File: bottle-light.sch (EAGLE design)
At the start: 55 parts, among them IC1 STM32F334K8T, IC2 LF33, X1 MINI-USB-SHIELD-UX60A-MB-5ST

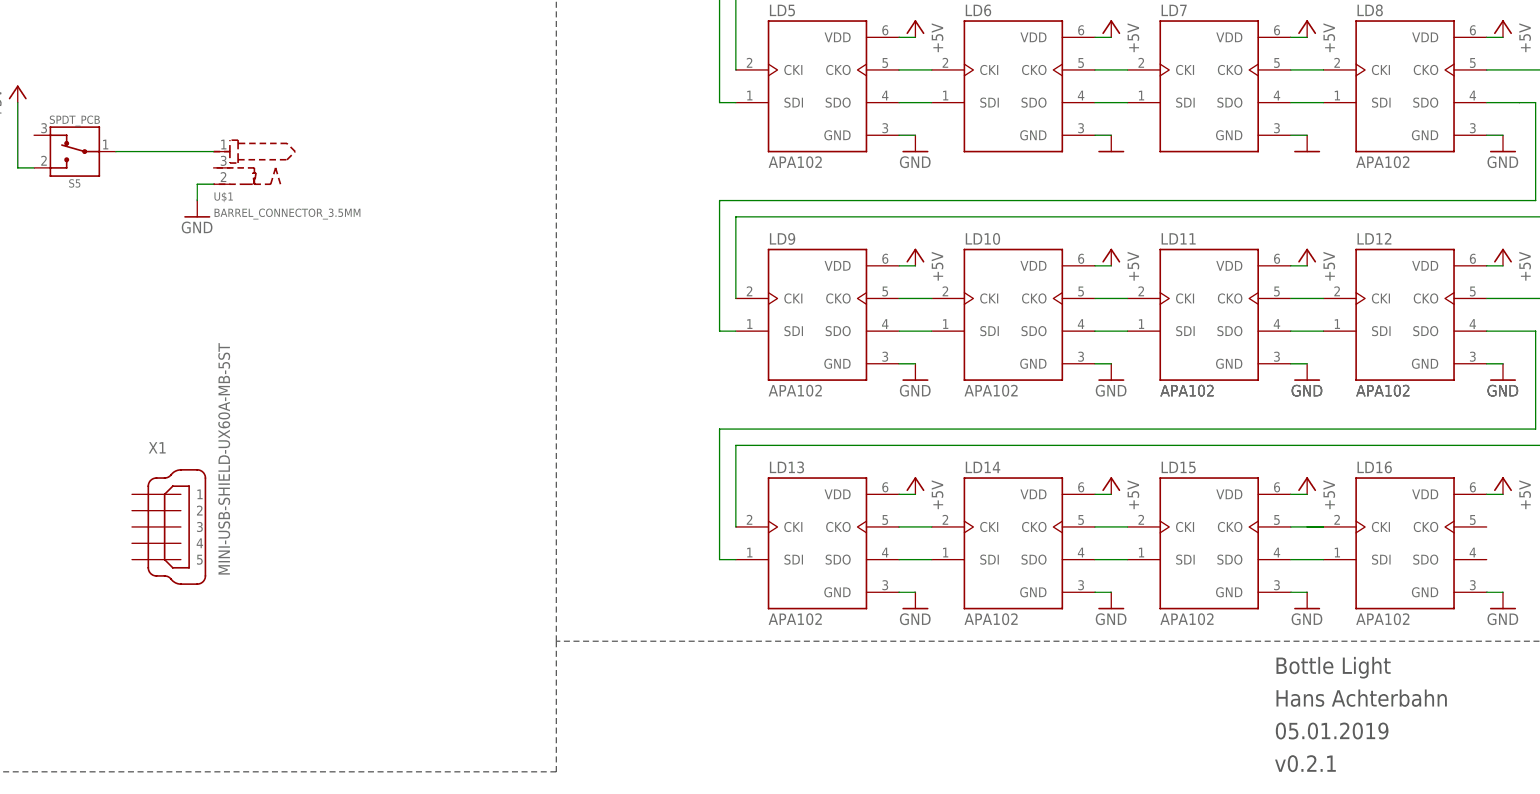
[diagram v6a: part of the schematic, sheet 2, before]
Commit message: v0.2.2 LEDs connected and port for touch pad added
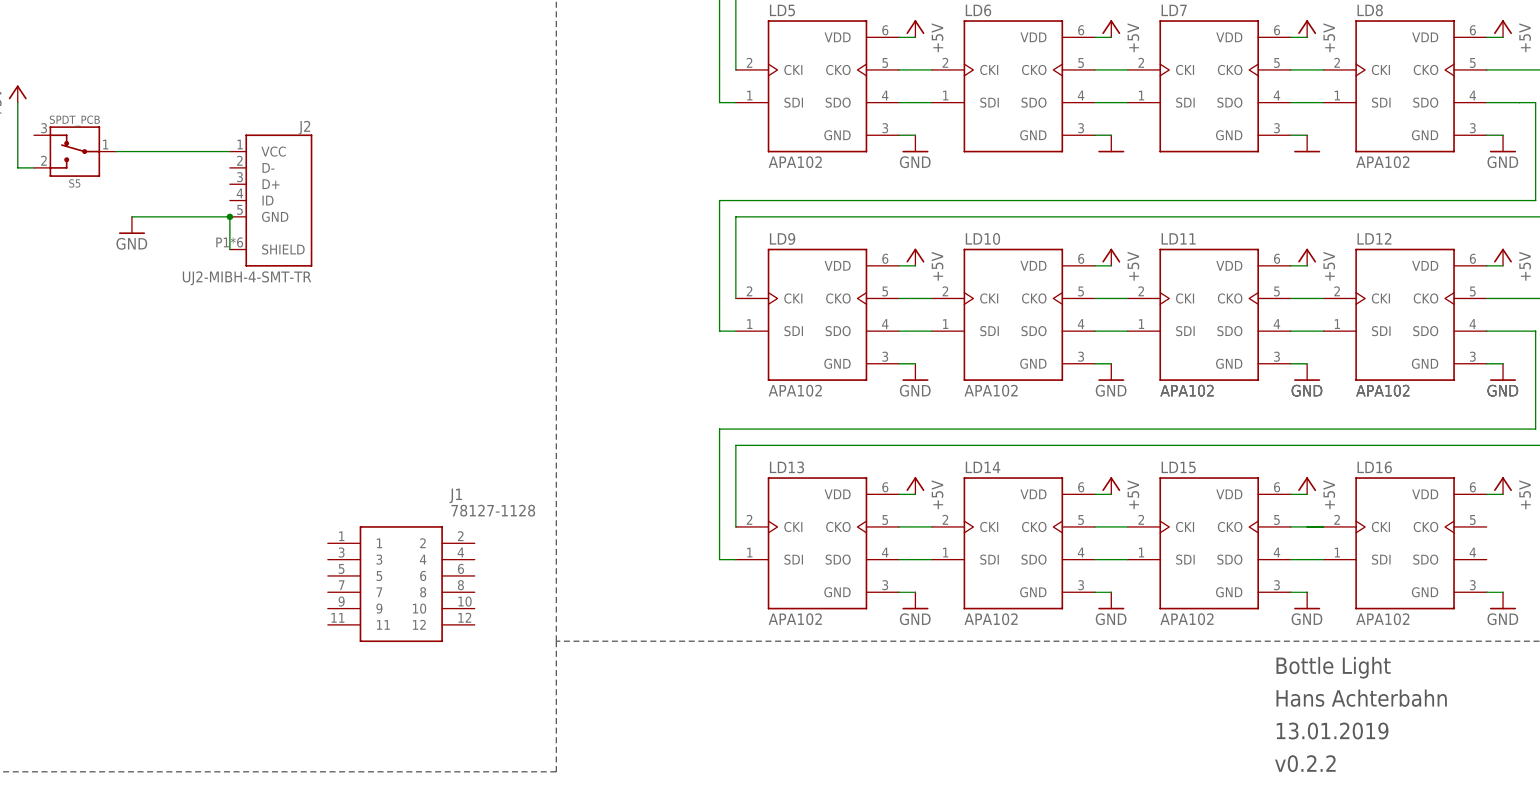
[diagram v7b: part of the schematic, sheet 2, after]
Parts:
- removed U$1: BARREL_CONNECTOR_3.5MM, h8-conector:BARREL_CONNECTOR_3.5MM
- removed X1: MINI-USB-SHIELD-UX60A-MB-5ST, con-hirose:MINI-USB-SHIELD-UX60A-MB-5ST
- added J1: 78127-1128, SamaSys:78127-1128
- added J2: UJ2-MIBH-4-SMT-TR, UJ2-MIBH-4-SMT-TR:UJ2-MIBH-4-SMT-TR
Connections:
- removed net N$76: S5.1, U$1.1
- new net 5V-IN: J2.VCC, S5.1
- net GND: now also J2.GND, J2.SHIELD; no longer U$1.2
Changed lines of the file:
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@@
 <schematic xreflabel="%F%N/%S.%C%R" xrefpart="/%S.%C%R">
 <attributes>
-<attribute name="DATE" value="05.01.2019"/>
+<attribute name="DATE" value="13.01.2019"/>
 <attribute name="EDITOR" value="Hans Achterbahn"/>
 <attribute name="PROJECT" value="Bottle Light"/>
-<attribute name="VERSION" value="v0.2.1"/>
+<attribute name="VERSION" value="v0.2.2"/>
 </attributes>
 <variantdefs>
@@
 <part name="S3" library="h8-switch" deviceset="ALPS-SKHH" device=""/>
 <part name="S4" library="h8-switch" deviceset="ALPS-SKHH" device=""/>
-<part name="U$1" library="h8-conector" deviceset="BARREL_CONNECTOR_3.5MM" device=""/>
 <part name="GND22" library="supply1" library_urn="urn:adsk.eagle:library:371" deviceset="GND" device=""/>
 <part name="JP1" library="h8-pinhead" deviceset="PINHD-2X3" device="_2.54-SMD" value="SWD">
@@
 <part name="P+18" library="supply1" library_urn="urn:adsk.eagle:library:371" deviceset="+5V" device=""/>
 <part name="P+19" library="supply1" library_urn="urn:adsk.eagle:library:371" deviceset="+5V" device=""/>
-<part name="X1" library="con-hirose" library_urn="urn:adsk.eagle:library:152" deviceset="MINI-USB-SHIELD-" device="UX60A-MB-5ST" package3d_urn="urn:adsk.eagle:package:7263/1"/>
 <part name="R1" library="resistor" deviceset="R-EU_" device="R0603" value="8.2">
 <attribute name="RS-ONLINE" value="904-5027"/>
@@
 <attribute name="RS-ONLINE" value="904-5027"/>
 </part>
+<part name="J1" library="SamaSys" deviceset="78127-1128" device=""/>
+<part name="J2" library="UJ2-MIBH-4-SMT-TR" deviceset="UJ2-MIBH-4-SMT-TR" device=""/>
 </parts>
 <sheets>
@@
 <attribute name="VALUE" x="10.16" y="106.68" size="1.778" layer="96" rot="R90"/>
 </instance>
-<instance part="GND10" gate="1" x="40.64" y="91.44" smashed="yes">
-<attribute name="VALUE" x="38.1" y="88.9" size="1.778" layer="96"/>
+<instance part="GND10" gate="1" x="30.48" y="88.9" smashed="yes">
+<attribute name="VALUE" x="27.94" y="86.36" size="1.778" layer="96"/>
 </instance>
 <instance part="GND12" gate="1" x="38.1" y="129.54" smashed="yes">
@@
 <attribute name="VALUE" x="21.59" y="105.918" size="1.27" layer="96" font="vector" rot="R180" align="top-center"/>
 </instance>
-<instance part="U$1" gate="G$1" x="43.18" y="101.6" smashed="yes">
-<attribute name="NAME" x="43.18" y="93.98" size="1.27" layer="95"/>
-<attribute name="VALUE" x="43.18" y="91.44" size="1.27" layer="96"/>
-</instance>
 <instance part="LD1" gate="G$1" x="137.16" y="147.32" smashed="yes">
 <attribute name="NAME" x="129.54" y="158.242" size="1.778" layer="95"/>
@@
 <attribute name="VALUE" x="246.38" y="45.72" size="1.778" layer="96" rot="MR90"/>
 </instance>
-<instance part="X1" gate="G$1" x="35.56" y="43.18" smashed="yes">
-<attribute name="NAME" x="33.02" y="54.61" size="1.778" layer="95"/>
-<attribute name="VALUE" x="45.72" y="35.56" size="1.778" layer="96" rot="R90"/>
+<instance part="J1" gate="G$1" x="60.96" y="40.64" smashed="yes">
+<attribute name="NAME" x="80.01" y="48.26" size="1.778" layer="95" align="center-left"/>
+<attribute name="VALUE" x="80.01" y="45.72" size="1.778" layer="96" align="center-left"/>
+</instance>
+<instance part="J2" gate="G$1" x="53.34" y="93.98" smashed="yes" rot="MR0">
+<attribute name="NAME" x="58.43228125" y="104.6738" size="1.68045" layer="95" rot="MR0"/>
+<attribute name="VALUE" x="58.428890625" y="81.2578" size="1.67933125" layer="96" rot="MR0"/>
 </instance>
 </instances>
@@
 </segment>
 <segment>
-<pinref part="U$1" gate="G$1" pin="2"/>
-<wire x1="43.18" y1="96.52" x2="40.64" y2="96.52" width="0.1524" layer="91"/>
-<wire x1="40.64" y1="96.52" x2="40.64" y2="93.98" width="0.1524" layer="91"/>
+<wire x1="45.72" y1="91.44" x2="30.48" y2="91.44" width="0.1524" layer="91"/>
 <pinref part="GND10" gate="1" pin="GND"/>
+<pinref part="J2" gate="G$1" pin="GND"/>
+<pinref part="J2" gate="G$1" pin="SHIELD"/>
+<wire x1="45.72" y1="91.44" x2="45.72" y2="86.36" width="0.1524" layer="91"/>
+<junction x="45.72" y="91.44"/>
 </segment>
 <segment>
@@
 </segment>
 </net>
-<net name="N$76" class="0">
-<segment>
-<pinref part="U$1" gate="G$1" pin="1"/>
-<wire x1="27.94" y1="101.6" x2="43.18" y2="101.6" width="0.1524" layer="91"/>
+<net name="5V-IN" class="0">
+<segment>
+<wire x1="27.94" y1="101.6" x2="45.72" y2="101.6" width="0.1524" layer="91"/>
 <pinref part="S5" gate="G$1" pin="1"/>
-</segment>
-</net>
+<pinref part="J2" gate="G$1" pin="VCC"/>
+</segment>
+</net>

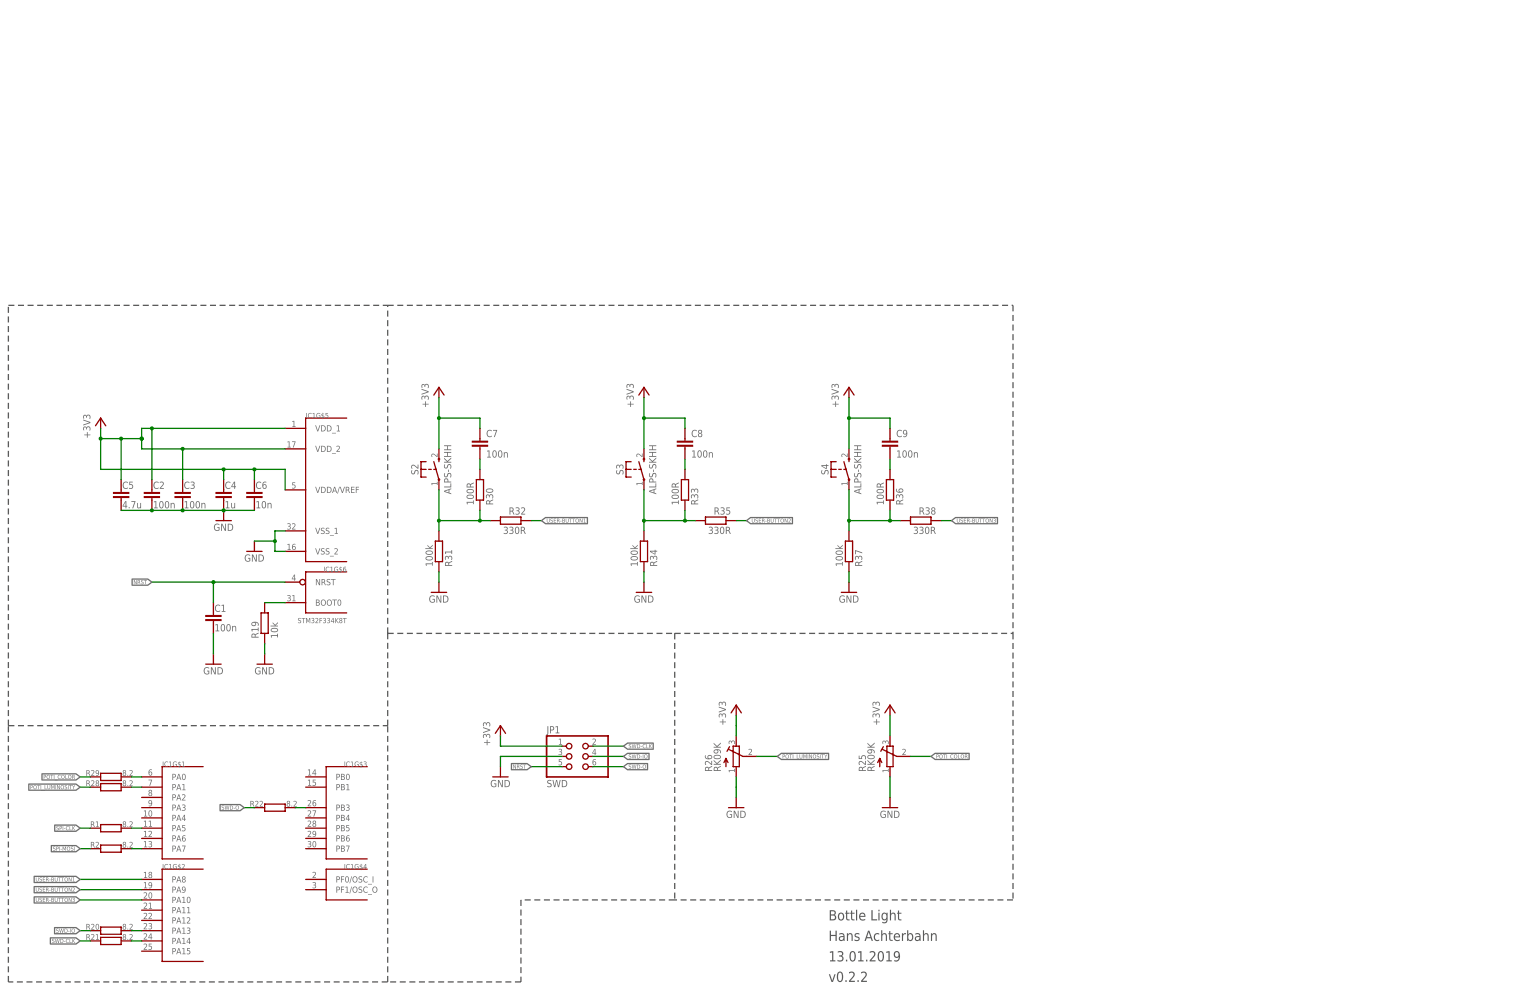
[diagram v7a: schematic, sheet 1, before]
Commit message: v0.2.3 pinout and connection of touch pad to STM32 | changed library of buttons and potentiometers | added polygon on top and bottom| changed Micro-USB position
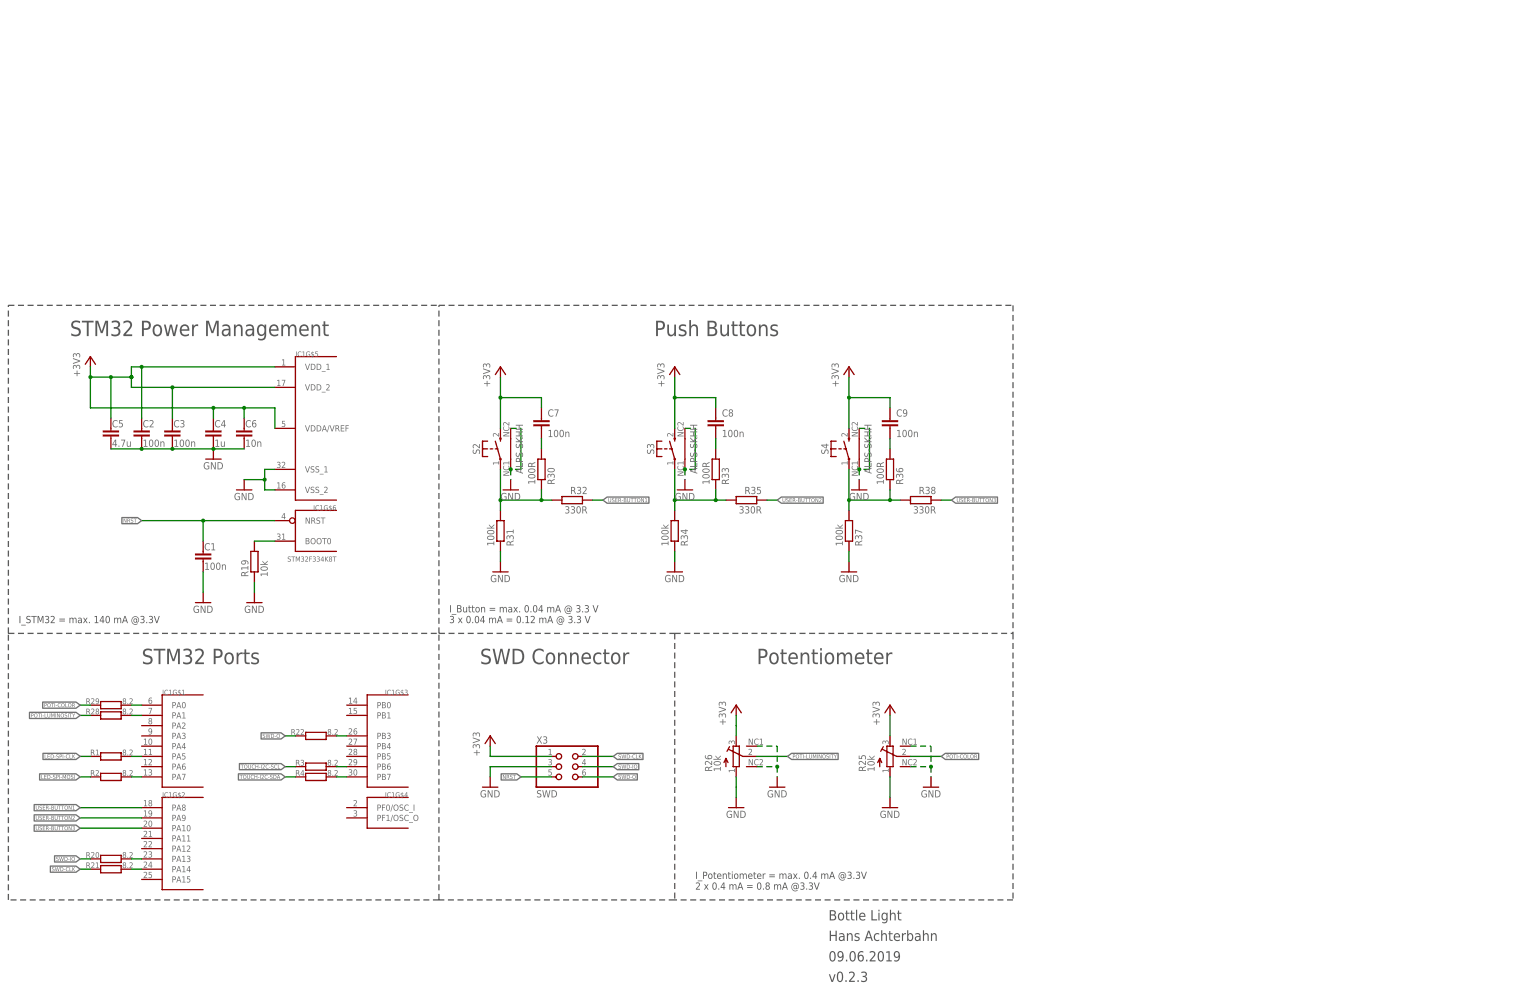
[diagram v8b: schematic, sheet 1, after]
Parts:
- removed J1: 78127-1128, SamaSys:78127-1128
- removed J2: UJ2-MIBH-4-SMT-TR, UJ2-MIBH-4-SMT-TR:UJ2-MIBH-4-SMT-TR
- removed JP1: SWD, h8-pinhead:PINHD-2X3_2.54-SMD
- added R3, R4: 8.2, resistor:R-EU_R0603
- added X1: 78127-1128, SamaSys:78127-1128
- added X2: UJ2-MIBH-4-SMT-TR, UJ2-MIBH-4-SMT-TR:UJ2-MIBH-4-SMT-TR
- added X3: SWD, h8-pinhead:PINHD-2X3_2.54-SMD
- R25, R26: value RK09K -> 10k
- S2: device h8-switch:ALPS-SKHH -> h8-switch:ALPS-SKHH-SHIELD; SPICEPREFIX (none) -> B
- S3, S4: device h8-switch:ALPS-SKHH -> h8-switch:ALPS-SKHH-SHIELD
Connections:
- net POTI_COLOR renamed POTI-COLOR
- net POTI_LUMINOSITY renamed POTI-LUMINOSITY
- net SPI-CLK renamed LED-SPI-CLK
- new net !TOUCH-SPI-SS: X1.3
- new net LED-SPI-MOSI: R2.1
- new net N$4: IC1G$3.PB6, R3.2
- new net N$5: IC1G$3.PB7, R4.2
- new net TOUCH-BTN1: X1.8
- new net TOUCH-BTN2: X1.6
- new net TOUCH-BTN3: X1.7
- new net TOUCH-DR: X1.4
- new net TOUCH-I2C-SCL: R3.1, X1.9
- new net TOUCH-I2C-SDA: R4.1, X1.10
- new net TOUCH-SPI-MISO: X1.2
- new net TOUCH-SPI-MOSI: X1.5
- new net TOUCH-SPI-SCK: X1.1
- net +3V3: now also X1.12, X3.1; no longer JP1.1
- net 5V-IN: now also X2.VCC; no longer J2.VCC
- net GND: now also R25.NC1, R25.NC2, R26.NC1, R26.NC2, S2.NC1, S2.NC2, S3.NC1, S3.NC2, S4.NC1, S4.NC2, X1.11, X2.GND, X2.SHIELD, X3.3; no longer J2.GND, J2.SHIELD, JP1.3
- net NRST: now also X3.5; no longer JP1.5
- net SPI-MOSI: no longer R2.1
- net SWD-CLK: now also X3.2; no longer JP1.2
- net SWD-IO: now also X3.4; no longer JP1.4
- net SWD-O: now also X3.6; no longer JP1.6
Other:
- note added: "5V to 3.3V"
- note added: "Delivers 0.5 A @ 3.3 V"
- note added: "I_APA102 = max. 27 mA @ 5 V 16 x 27 mA = 0.432 A @ 5 V"
- note added: "I_Button = max. 0.04 mA @ 3.3 V 3 x 0.04 mA = 0.12 mA @ 3.3 V"
- note added: "I_Potentiometer = max. 0.4 mA @3.3V 2 x 0.4 mA = 0.8 mA @3.3V"
- note added: "I_STM32 = max. 140 mA @3.3V"
- note added: "I_Touchpad = max. 3 mA @ 3.3 V"
- note added: "Potentiometer"
- note added: "Power supply by Micro-USB"
- note added: "Push Buttons"
- note added: "RGB LED - APA102"
- note added: "STM32 Ports"
- note added: "STM32 Power Management"
- note added: "SWD Connector"
- note added: "Touchpad connector"
- note added: "Touchpad: TM023023-2024-002 @ Cirque"
- note added: "Use a micro-USB connector that supplies at least 1A of current."
- moved on the sheet: C1, C12, C13, C2, C3, C4, C5, C6, C7, C8, C9, IC1G$1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
